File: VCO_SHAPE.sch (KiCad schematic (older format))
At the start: 52 parts, among them U501 TL074, U502 LM13700, U503 TL074

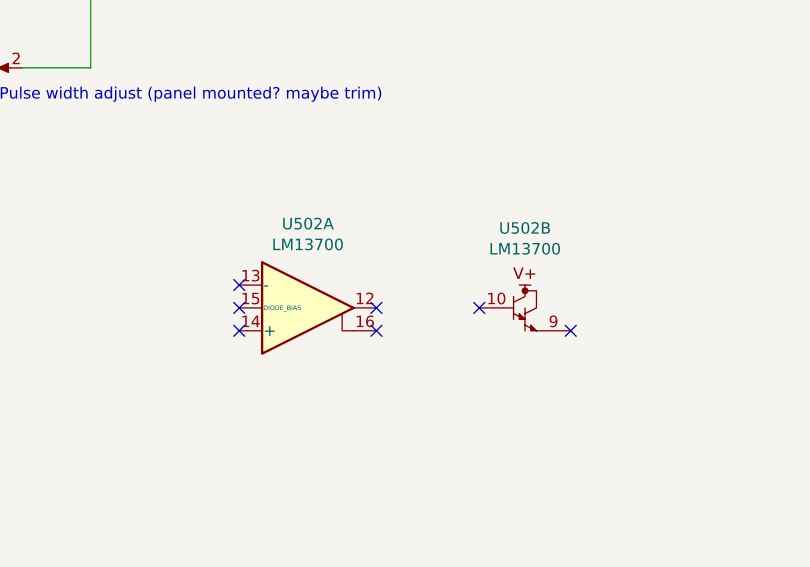
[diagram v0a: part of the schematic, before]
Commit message: deleted extra lm13700
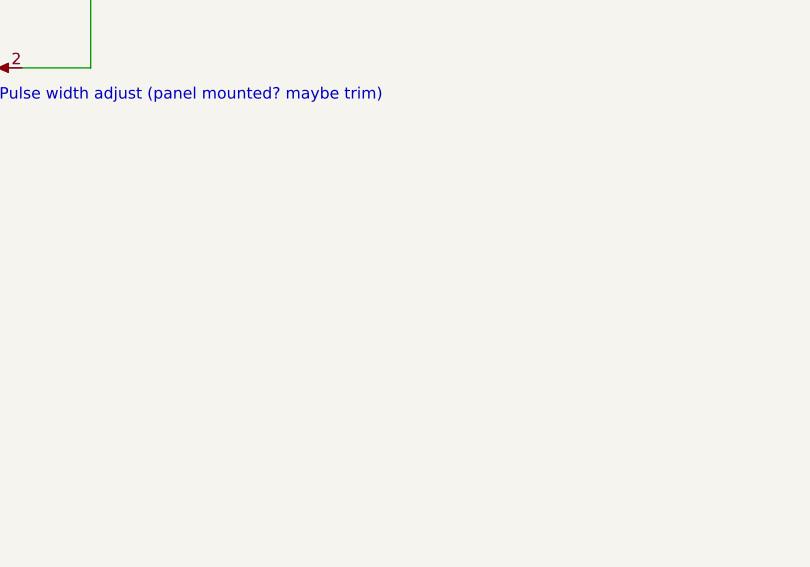
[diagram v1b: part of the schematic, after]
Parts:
- removed unit 1 of U502
- removed unit 2 of U502
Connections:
- no-connect marks 8 -> 1
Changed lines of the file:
@@
-$Comp
-L Amplifier_Operational:LM13700 U502
-U 1 1 604F143D
-P 9100 5150
-F 0 "U502" H 9100 5517 50  0000 C CNN
-F 1 "LM13700" H 9100 5426 50  0000 C CNN
-F 2 "Package_DIP:DIP-16_W7.62mm" H 8800 5175 50  0001 C CNN
-F 3 "http://www.ti.com/lit/ds/symlink/lm13700.pdf" H 8800 5175 50  0001 C CNN
-	1    9100 5150
-	1    0    0    -1
-$EndComp
-$Comp
-L Amplifier_Operational:LM13700 U502
-U 2 1 604F4C10
-P 10150 5150
-F 0 "U502" H 10050 5498 50  0000 C CNN
-F 1 "LM13700" H 10050 5407 50  0000 C CNN
-F 2 "Package_DIP:DIP-16_W7.62mm" H 9850 5175 50  0001 C CNN
-F 3 "http://www.ti.com/lit/ds/symlink/lm13700.pdf" H 9850 5175 50  0001 C CNN
-	2    10150 5150
-	1    0    0    -1
-$EndComp
 $Comp
 L Amplifier_Operational:LM13700 U502
@@
 	-1   0    0    1
 $EndComp
-NoConn ~ 9850 5150
-NoConn ~ 10250 5250
-NoConn ~ 9400 5250
-NoConn ~ 9400 5150
-NoConn ~ 8800 5250
-NoConn ~ 8800 5150
-NoConn ~ 8800 5050
 Wire Wire Line
 	10800 1650 10800 1750
